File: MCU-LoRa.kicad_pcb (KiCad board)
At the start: 2 copper layers, 48.3 x 71.1 mm, 46 parts, among them J1 Conn_01x01_Socket, J2 Conn_01x01_Socket, J3 Conn_01x01_Socket, J4 Conn_01x01_Socket, J5 Conn_01x01_Socket, J6 Conn_01x01_Socket, J7 Conn_01x01_Socket, J8 Conn_01x01_Socket, J9 Conn_02x04_Top_Bottom, SW1 SW_Push, SW2 SW_Push, U1 RFM95W-915S2, U2 STM32F411CEU6, Y1 32.758kHz, Y2 25MHz

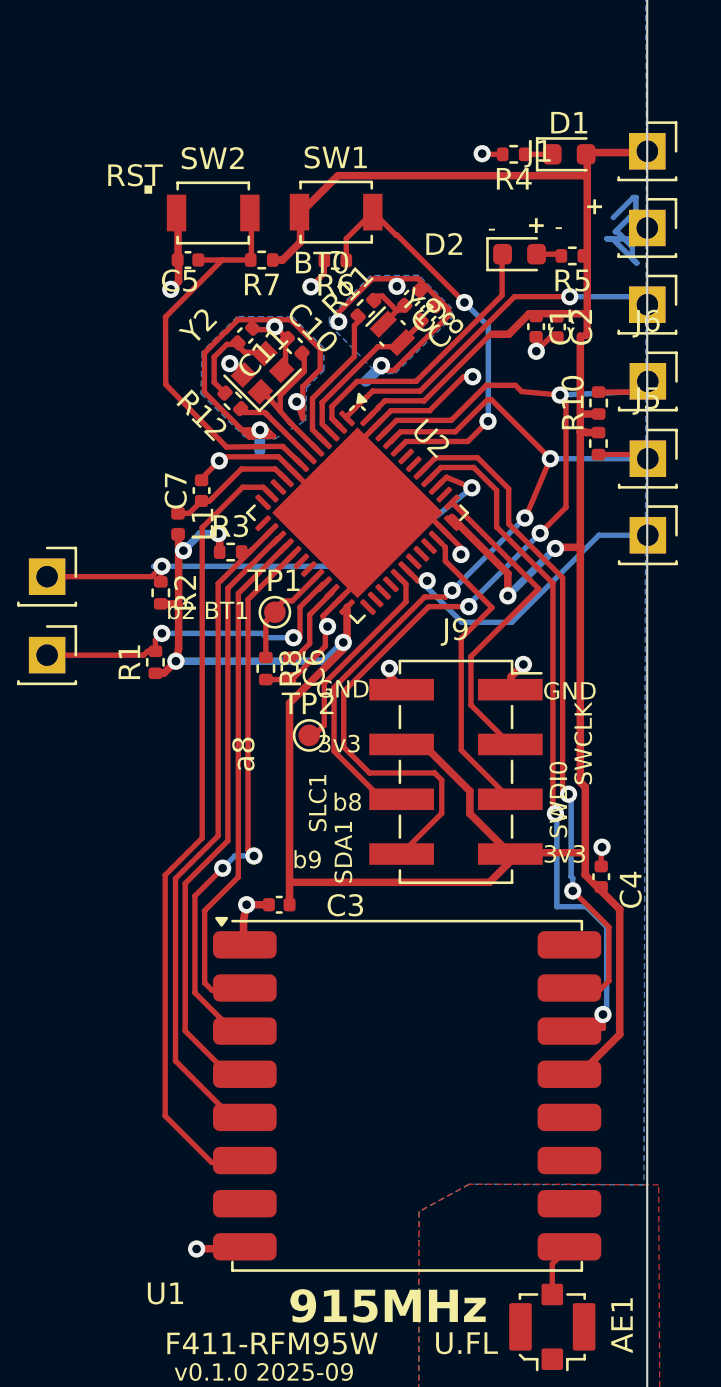
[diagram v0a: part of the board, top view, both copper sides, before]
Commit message: changed from vias to microvias. ERC ok. DRC has only warnings related to castellated edges cutting footprints.
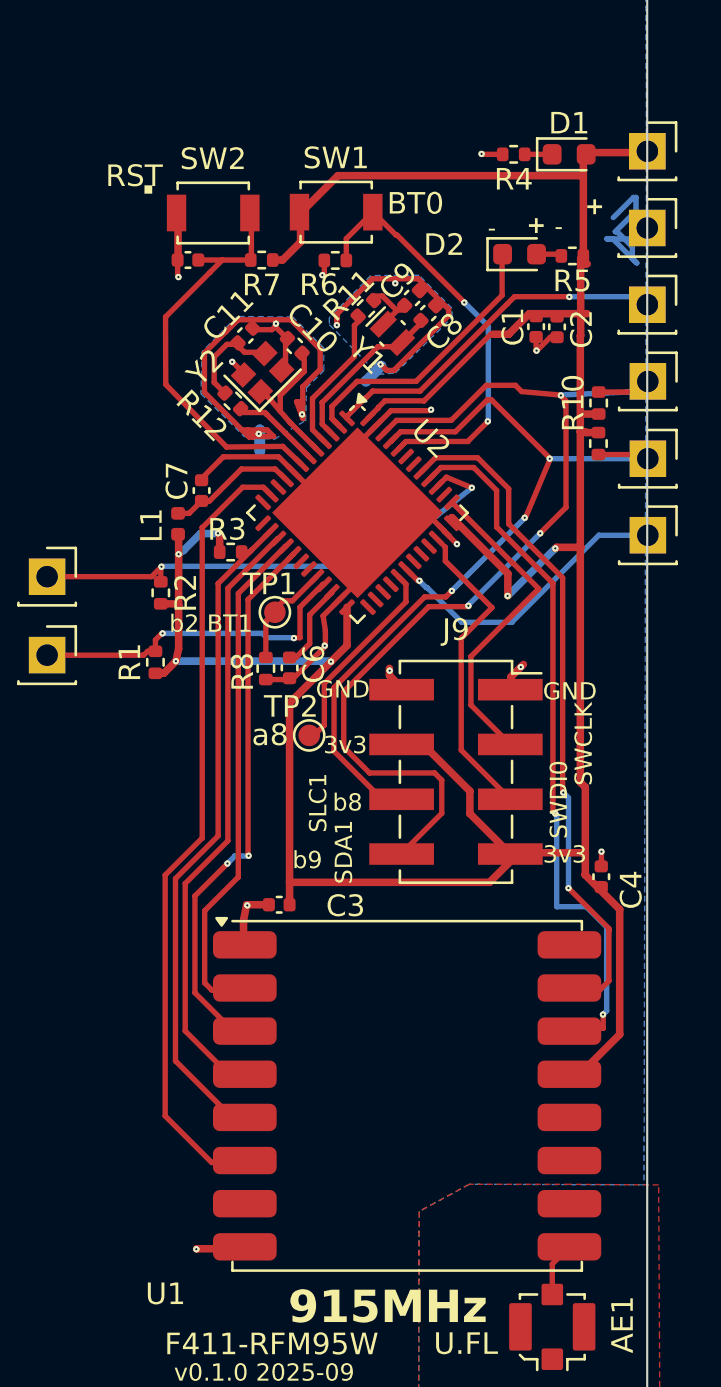
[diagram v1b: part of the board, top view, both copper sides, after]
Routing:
- net GND: track 49.0 -> 44.2 mm, vias 13 -> 12
- net +3V3: track 141.4 -> 140.7 mm

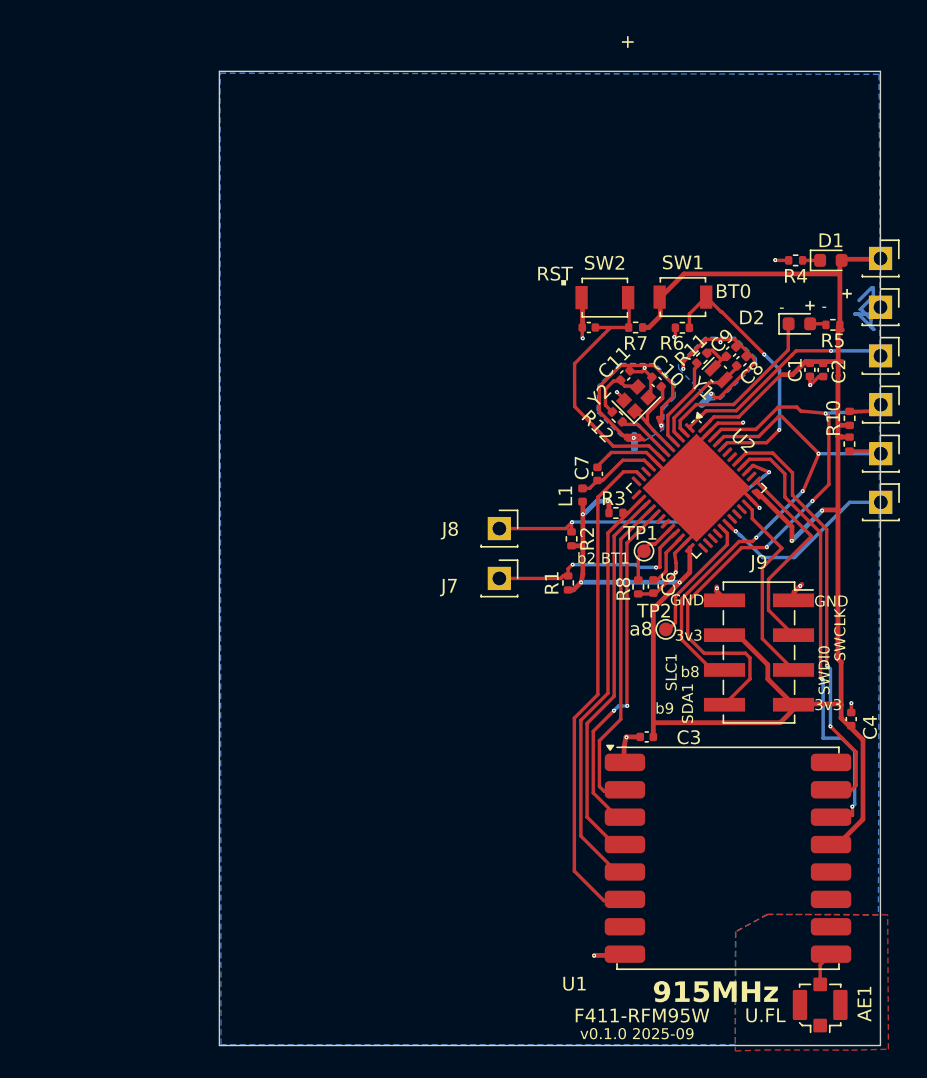
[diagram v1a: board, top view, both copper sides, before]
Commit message: 3v3 trace moved to back side.
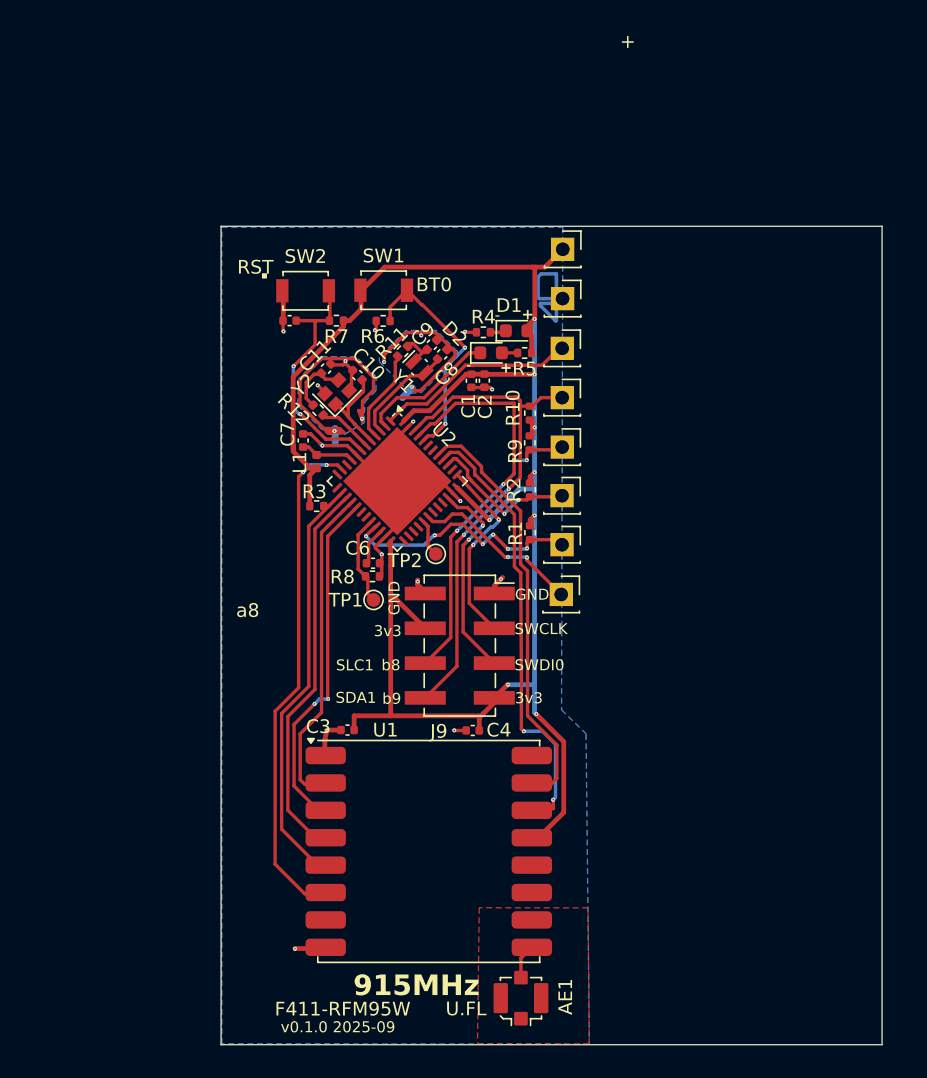
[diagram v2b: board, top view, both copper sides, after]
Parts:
- U2: footprint Package_DFN_QFN:QFN-48-1EP_7x7mm_P0.5mm_EP5.6x5.6mm -> ProjectLib:QFN-48-1EP_7x7mm_P0.5mm_EP5.6x5.6mm
- moved C4 27.6 mm to (68.0, 72.2), turned to 180 degrees
- moved C2 24.7 mm to (68.9, 46.7)
- moved C1 24.7 mm to (67.9, 46.7)
- moved J4 24.3 mm to (74.5, 62.3)
- moved D1 23.5 mm to (71.2, 43.1)
- moved R4 23.4 mm to (68.8, 43.2)
- moved R10 23.3 mm to (72.2, 49.1)
- moved R9 23.3 mm to (72.2, 51.2)
- moved J6 23.3 mm to (74.6, 48.0)
- moved J5 23.3 mm to (74.6, 51.6)
- moved J3 23.3 mm to (74.6, 44.4)
- moved J2 23.2 mm to (74.6, 40.7)
- moved J1 23.2 mm to (74.6, 37.1)
- moved D2 22.6 mm to (69.4, 44.7)
- moved R5 22.6 mm to (71.8, 44.7)
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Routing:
- net SDA2: track 23.8 -> 11.0 mm
- net SDA1: track 45.6 -> 37.0 mm, vias 3 -> 2
- net Net-(U2-PA8): track 9.27 -> 2.73 mm
- net +3V3: track 140.7 -> 137.2 mm, vias 6 -> 8
- net SCL1: track 36.8 -> 33.6 mm, vias 3 -> 4
- net GND: track 44.2 -> 41.1 mm, vias 12 -> 13
- net Net-(D2-K): track 13.6 -> 10.6 mm
- net SCL2: track 15.5 -> 17.7 mm, vias 2 -> 6
- net Net-(U2-VDDA/VREF+): track 6.05 -> 3.95 mm
- net Net-(U2-BOOT0): track 19.3 -> 17.5 mm
- net VBAT: track 16.4 -> 14.6 mm, vias 1 -> 0
- net Net-(U2-PB2): track 4.86 -> 6.51 mm
- net Net-(U2-VCAP1): track 4.15 -> 2.69 mm
- net Net-(U2-NRST): track 19.1 -> 17.7 mm, vias 0 -> 2
- net PA9: track 13.7 -> 12.6 mm, vias 1 -> 2
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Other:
- board size 48.3 x 71.1 mm -> 48.3 x 59.8 mm
- board text removed: "b2 BT1"

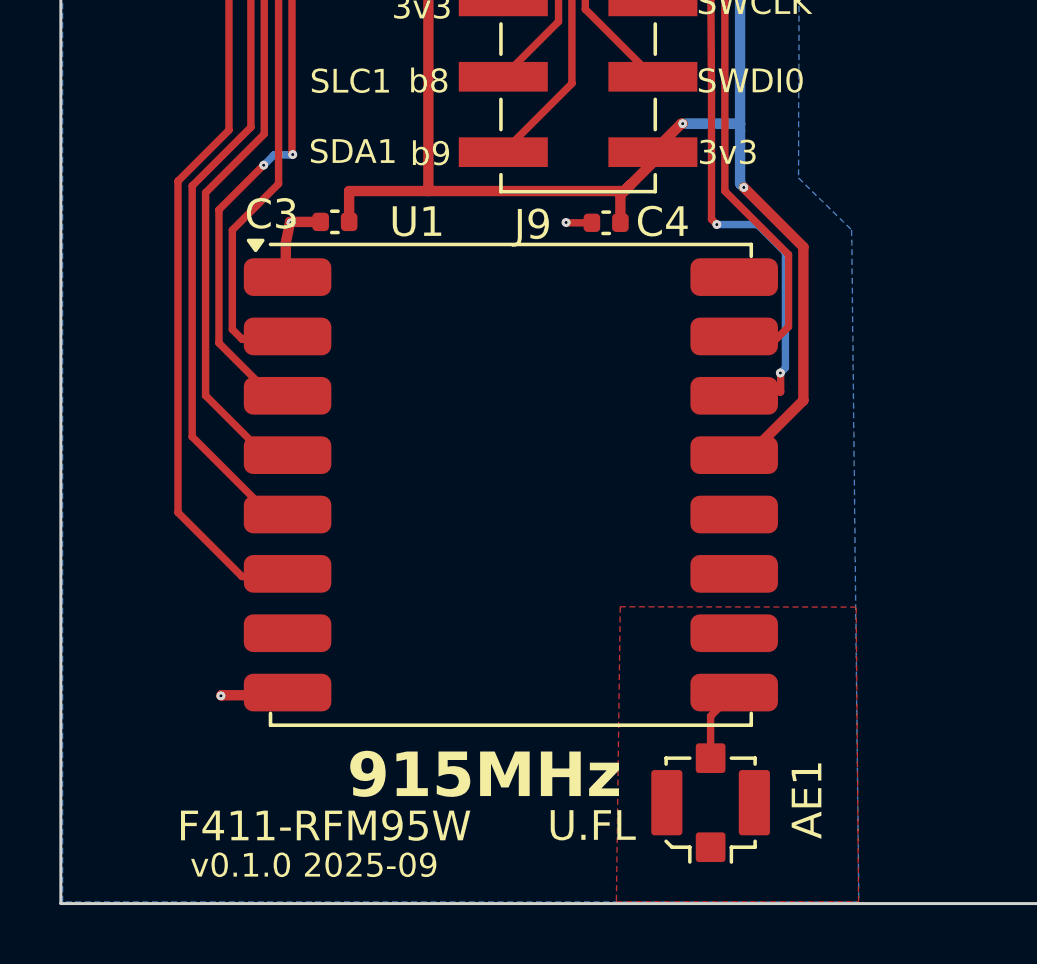
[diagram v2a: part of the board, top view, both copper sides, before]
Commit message: move antenna U.FL closer to corner.
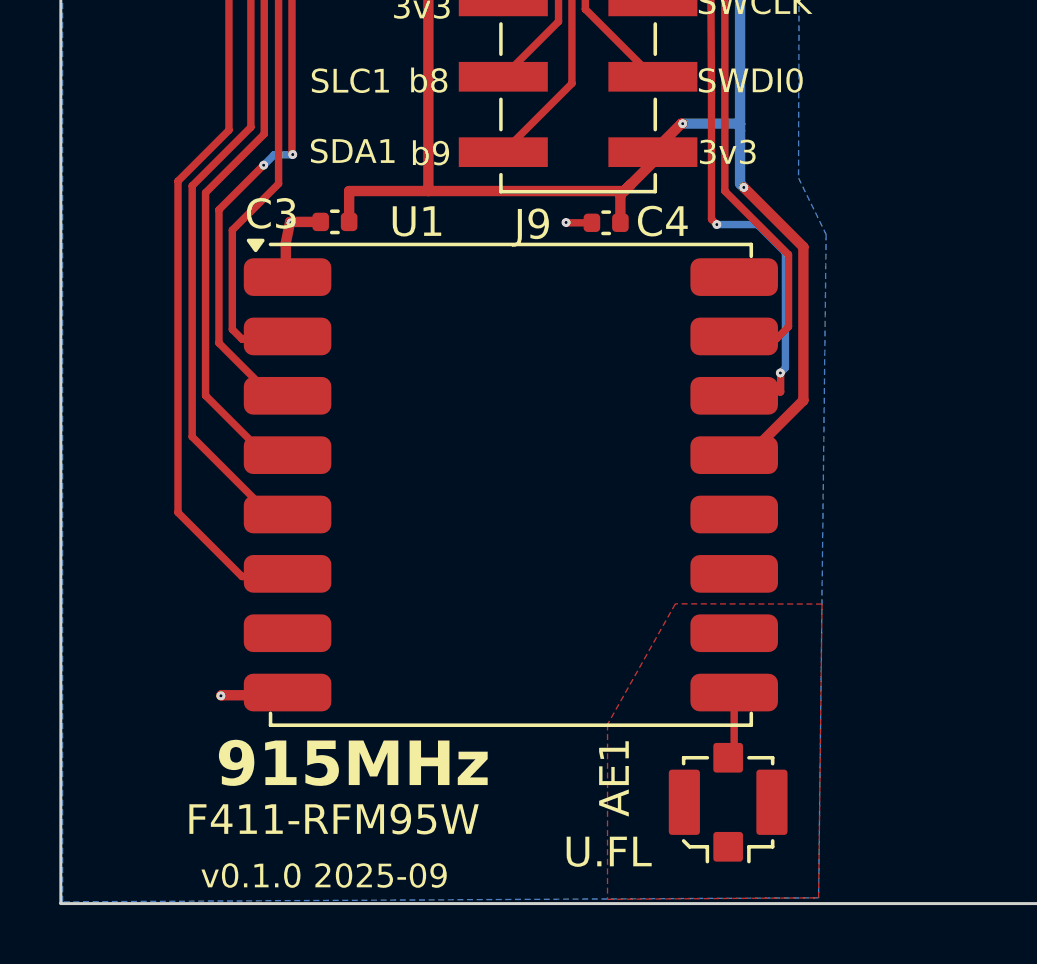
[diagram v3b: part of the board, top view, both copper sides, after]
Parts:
- moved AE1 0.59 mm to (72.1, 91.8)
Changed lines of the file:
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@@
 	(footprint "ProjectLib:U.FL_Molex_MCRF_73412-0110_Vertical"
 		(layer "F.Cu")
-		(at 71.545 91.79 180)
+		(at 72.136 91.776685 180)
 		(descr "Molex Microcoaxial RF Connectors (MCRF), mates Hirose U.FL, (http://www.molex.com/pdm_docs/sd/734120110_sd.pdf)")
 		(tags "mcrf hirose ufl u.fl microcoaxial")
 		(property "Reference" "AE1"
-			(at -3.27 0.11 90)
+			(at 3.81 0.844685 90)
 			(layer "F.SilkS")
 			(effects
@@
 		)
 		(property "Value" "U.FL"
-			(at 4.01 -0.79 0)
+			(at 4.064797 -1.695315 0)
 			(layer "F.SilkS")
 			(effects
@@
 	)
 	(gr_text "915MHz"
-		(at 59.295 91.75 0)
+		(at 54.87 91.38 0)
 		(layer "F.SilkS")
 		(effects
@@
 	)
 	(gr_text "v0.1.0 2025-09"
-		(at 54.005 94.38 0)
+		(at 54.356 94.742 0)
 		(layer "F.SilkS")
 		(effects
@@
 	)
 	(gr_text "F411-RFM95W"
-		(at 53.565 93.18 0)
+		(at 53.848 92.964 0)
 		(layer "F.SilkS")
 		(effects
@@
 	)
 	(segment
-		(start 72.34 88.08)
-		(end 71.545 88.875)
+		(start 72.34 90.072685)
+		(end 72.136 90.276685)
 		(width 0.25)
 		(layer "F.Cu")
@@
 	)
 	(segment
-		(start 71.545 88.875)
-		(end 71.545 90.29)
+		(start 72.34 88.08)
+		(end 72.34 90.072685)
 		(width 0.25)
 		(layer "F.Cu")
@@
 		(polygon
 			(pts
-				(xy 68.37 95.13) (xy 76.54 95.13) (xy 76.53 95.13) (xy 76.45 85.2) (xy 68.5 85.19)
+				(xy 68.071203 95.047603) (xy 75.184 94.996) (xy 75.299003 85.0975) (xy 70.358 85.09) (xy 68.072 89.154)
 			)
 		)
@@
 			(pts
 				(arc
-					(start 70.338522 91.783551)
-					(mid 72.706982 91.783551)
-					(end 70.338522 91.783551)
+					(start 70.935113 91.79709)
+					(mid 73.303573 91.79709)
+					(end 70.935113 91.79709)
 				)
 			)
@@
 		(polygon
 			(pts
-				(xy 74.6 35.51) (xy 74.50868 70.742732) (xy 76.29868 72.492732) (xy 76.54 95.14) (xy 49.70868 95.132732)
+				(xy 74.6 35.51) (xy 74.50868 70.742732) (xy 75.438 72.644) (xy 75.184 94.996) (xy 49.70868 95.132732)
 				(xy 49.71 95.13) (xy 49.71 35.5)
 			)

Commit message: ongoing
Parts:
- TP1: value BT1 b2 -> TP1
- moved J7 22.4 mm to (54.2, 68.2)
- moved R6 21.2 mm to (70.4, 61.6), turned to 0 degrees
- moved SW1 20.6 mm to (70.6, 58.6), turned to -90 degrees
- moved R1 17.2 mm to (56.8, 65.3)
- moved J3 16.2 mm to (74.5, 60.5)
- moved D2 14.8 mm to (65.9, 59.1), turned to 90 degrees
- moved J9 14.7 mm to (65.8, 51.4), turned to 90 degrees
- moved R11 14.4 mm to (62.0, 59.0), turned to 90 degrees
- moved D1 13.9 mm to (58.5, 48.7), turned to 180 degrees
- moved R5 13.6 mm to (66.1, 57.0)
- moved C7 13.5 mm to (59.3, 64.1)
- moved C5 13.4 mm to (58.3, 55.2), turned to 90 degrees
- moved R12 13.3 mm to (59.4, 61.9), turned to 180 degrees
- moved Y1 13.2 mm to (63.7, 58.9), turned to 0 degrees
- moved C9 13.1 mm to (63.2, 57.0), turned to -90 degrees
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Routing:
- net +3V3: track 137.2 -> 114.4 mm, vias 8 -> 12
- net SDA1: track 37.0 -> 15.5 mm
- net GND: track 41.1 -> 58.2 mm, vias 13 -> 12
- net SCL1: track 33.6 -> 20.6 mm, vias 4 -> 0
- net RESET: track 37.0 -> 24.3 mm
- net DIO0: track 32.9 -> 20.5 mm
- net MOSI: track 25.3 -> 13.0 mm
- net DIO1: track 31.2 -> 19.1 mm
- net NSS: track 30.7 -> 19.0 mm
- net Net-(U2-BOOT0): track 17.5 -> 6.04 mm, vias 2 -> 0
- net /f411/SWDIO: track 15.2 -> 26.3 mm
- net MISO: track 23.8 -> 12.8 mm
- net /f411/SWCLK: track 14.4 -> 25.4 mm
- net SCK: track 27.6 -> 17.3 mm
- net GND_HSE: track 23.4 -> 16.7 mm, vias 4 -> 5
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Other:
- board text removed: "-"
- board text removed: "."
- board text removed: "BT0"
- board text removed: "RST"

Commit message: MCU moved down closer to radio. Connectors need better arrangement.
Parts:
- TP1: value TP1 -> BT1 b2
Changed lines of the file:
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@@
 		(sheetname "/f411/")
 		(sheetfile "f411.kicad_sch")
-		(attr exclude_from_pos_files dnp)
+		(attr exclude_from_pos_files exclude_from_bom dnp)
 		(fp_circle
 			(center 0 0)
@@
 			(layers "F.Cu" "F.Mask" "F.Paste")
 			(net 2 "GND")
+			(pinfunction "Pin_a1")
+			(pintype "passive")
 		)
 		(pad "a2" smd rect
@@
 			(layers "F.Cu" "F.Mask" "F.Paste")
 			(net 1 "+3V3")
+			(pinfunction "Pin_a2")
+			(pintype "passive")
 		)
 		(pad "a3" smd rect
@@
 			(layers "F.Cu" "F.Mask" "F.Paste")
 			(net 36 "SCL1")
+			(pinfunction "Pin_a3")
+			(pintype "passive")
 		)
 		(pad "a4" smd rect
@@
 			(layers "F.Cu" "F.Mask" "F.Paste")
 			(net 35 "SDA1")
+			(pinfunction "Pin_a4")
+			(pintype "passive")
 		)
 		(pad "b1" smd rect
@@
 			(layers "F.Cu" "F.Mask" "F.Paste")
 			(net 2 "GND")
+			(pinfunction "Pin_b1")
+			(pintype "passive")
 		)
 		(pad "b2" smd rect
@@
 			(layers "F.Cu" "F.Mask" "F.Paste")
 			(net 37 "/f411/SWCLK")
+			(pinfunction "Pin_b2")
+			(pintype "passive")
 		)
 		(pad "b3" smd rect
@@
 			(layers "F.Cu" "F.Mask" "F.Paste")
 			(net 34 "/f411/SWDIO")
+			(pinfunction "Pin_b3")
+			(pintype "passive")
 		)
 		(pad "b4" smd rect
@@
 			(layers "F.Cu" "F.Mask" "F.Paste")
 			(net 1 "+3V3")
+			(pinfunction "Pin_b4")
+			(pintype "passive")
 		)
 		(embedded_fonts no)
@@
 			)
 		)
-		(property "Value" "TP1"
+		(property "Value" "BT1  b2"
 			(at 0 0 0)
 			(layer "F.SilkS")

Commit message: ongoing
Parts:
- removed J1, J2, J3, J4, J5, J6: Conn_01x01_Socket, ProjectLib:PinSocket_1x01_P2.54mm_Vertical
- J7, J8: value Conn_01x01_Socket -> Conn_01x08_Pin; footprint ProjectLib:PinSocket_1x01_P2.54mm_Vertical -> ProjectLib:castellated_1x08_P2.54mm
- TP2: value TestPoint_Probe -> MCO
- U2: footprint ProjectLib:QFN-48-1EP_7x7mm_P0.5mm_EP5.6x5.6mm -> Package_DFN_QFN:QFN-48-1EP_7x7mm_P0.5mm_EP5.6x5.6mm
- moved J7 10.2 mm to (49.6, 59.1), turned to 90 degrees
- moved J8 5.42 mm to (72.5, 59.1), turned to -90 degrees
- moved R3 3.59 mm to (54.4, 69.1)
- moved C3 3.35 mm to (66.8, 71.5)
- moved C4 3.35 mm to (68.3, 62.7)
- moved C8 3.35 mm to (60.8, 57.1)
- moved R6 3.35 mm to (67.0, 61.7)
- moved R9 3.35 mm to (68.8, 55.3)
- moved TP2 3.35 mm to (65.0, 70.9)
- moved C1 3.35 mm to (56.0, 55.3)
- moved C10 3.35 mm to (56.4, 57.7)
- moved C11 3.35 mm to (54.9, 57.7)
- moved C5 3.35 mm to (55.0, 55.3)
- moved C6 3.35 mm to (58.0, 71.1)
- moved C7 3.35 mm to (55.9, 64.2)
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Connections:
- J7 pad 1: SCL2 -> GND
- J8 pad 1: SDA2 -> +3V3
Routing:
- net GND: track 58.2 -> 34.3 mm, vias 12 -> 11
- net PA9: track 9.33 -> 14.4 mm, vias 1 -> 2
- net SCL2: track 11.8 -> 14.6 mm
- net SDA1: track 15.5 -> 17.4 mm
- net SDA2: track 10.6 -> 11.9 mm
- net SCL1: track 20.6 -> 21.8 mm
- net +3V3: track 114.4 -> 115.2 mm, vias 12 -> 11
- net VBAT: track 13.6 -> 14.4 mm
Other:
- board size 48.3 x 59.8 mm -> 22.9 x 49 mm
- board text added: "A"
- board text added: "DI0"
- board text added: "K"
- board text added: "SWK"
- board text removed: "SWCLK"
- board text removed: "SWDI0"
